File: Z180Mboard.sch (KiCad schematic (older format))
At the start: 66 parts, among them J1 Conn_02x05_Odd_Even, J10 PS2-MINIDIN6-FEMALE-SINGLE, J11 Conn_02x04_Odd_Even, J12 Conn_01x06, J13 Conn_01x06, J14 Conn_02x10_Top_Bottom, J15 Conn_02x05_Odd_Even, J16 DB9_Female, J17 Conn_01x40, J2 Conn_02x05_Odd_Even, J3 Conn_02x05_Odd_Even, J4 Conn_02x05_Odd_Even, J5 Conn_02x05_Odd_Even, J6 Conn_02x05_Odd_Even, J7 Conn_02x05_Odd_Even, J8 Conn_01x08, J9 PS2-MINIDIN6-FEMALE-SINGLE, SW1 SW_SPST, SW2 SW_Push, U1 Z8-L180-S180-180-PLCC-68, U10 74LVC245, U11 DS1307+, U2 SST39SF040, U3 74AHCT138, U4 74AHCT139, U5 AS6C4008-55PCN, U6 AS6C4008-55PCN, U7 82C55A_PLCC, U8 74HCT138, U9 74AHCT151, X1 CXO_DIP8, Y1 Crystal

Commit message: z180mboard: Add the floppy disk interface
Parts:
- added C12, C13, C14: 0.1uF, Capacitor_THT:C_Disc_D3.0mm_W2.0mm_P2.50mm, symbol Device:C
- added J18: Conn_02x17_Odd_Even, Connector_IDC:IDC-Header_2x17_P2.54mm_Vertical, symbol Connector_Generic:Conn_02x17_Odd_Even
- added J19: Conn_01x03, Connector_PinHeader_2.54mm:PinHeader_1x03_P2.54mm_Vertical, symbol Connector_Generic:Conn_01x03
- added JP3: Jumper_3_Open, Connector_PinHeader_2.54mm:PinHeader_1x03_P2.54mm_Vertical, symbol Jumper:Jumper_3_Open
- added R10, R11, R12, R8, R9: 1K, Resistor_THT:R_Axial_DIN0207_L6.3mm_D2.5mm_P7.62mm_Horizontal, symbol Device:R
- added U12: WD37C65C-DIP44, Package_LCC:PLCC-44_THT-Socket, symbol AlanMisc:WD37C65C-DIP44
- added U13: 74HCT138, Package_DIP:DIP-16_W7.62mm_Socket, symbol 74xx:74LS138
- added U14: 74HCT00, Package_DIP:DIP-14_W7.62mm_Socket, symbol 74xx:74HCT00
- added X2: CXO_DIP8, Oscillator:Oscillator_DIP-8, symbol Oscillator:CXO_DIP8
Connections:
- net A0: now also U12.4 (A0), U13.1 (A0)
- net A1: now also U13.2 (A1)
- net A2: now also U13.3 (A2)
- net D0: now also U12.7 (DB0)
- net D1: now also U12.8 (DB1)
- net D2: now also U12.9 (DB2)
- net D3: now also U12.10 (DB3)
- net D4: now also U12.11 (DB4)
- net D5: now also U12.12 (DB5)
- net D6: now also U12.13 (DB6)
- net D7: now also U12.14 (DB7)
- net GND: now also C12.2, C13.2, C14.2, J18.1 (Pin_1), J18.11 (Pin_11), J18.13 (Pin_13), J18.15 (Pin_15), J18.17 (Pin_17), J18.19 (Pin_19), J18.21 (Pin_21), J18.23 (Pin_23), J18.25 (Pin_25), J18.27 (Pin_27), J18.29 (Pin_29), J18.31 (Pin_31), J18.33 (Pin_33), J18.5 (Pin_5), J18.7 (Pin_7), J18.9 (Pin_9), J19.1 (Pin_1), JP3.3 (B), U12.17 (DCHGEN), U12.34 (VSS), U13.4 (E1), U13.8 (GND), U14.12, U14.13, U14.7 (GND), X2.4 (GND)
- net RD: now also U12.1 (RD)
- net RESET: now also U14.9
- net VCC: now also C12.1, C13.1, C14.1, J19.3 (Pin_3), JP3.1 (A), R10.1, R11.1, R12.1, R8.1, R9.1, U12.27 (PCVAL), U12.44 (VCC), U12.6 (TC), U13.16 (VCC), U13.6 (E3), U14.14 (VCC), X2.8 (Vcc)
- net WR: now also U12.2 (WR)
- net FDCEN: now reaches U3.9 (O6)
- net FDCEN: now also U13.5 (E2)
- new net: U12.18 (LDOR), U13.13 (O2)
- new net: U12.19 (LDCR), U13.12 (O3)
- new net: U12.20 (RST), U14.8
- new net: JP3.2 (C), U12.24 (DRV)
- new net: U12.3 (CS), U14.6
- new net: U12.5 (DACK), U13.11 (O4)
- new net: U13.10 (O5), U14.10
- new net: U13.14 (O1), U14.2
- new net: U13.15 (O0), U14.1
- new net: U14.3, U14.4, U14.5
- new net DIR: J18.18 (Pin_18), U12.31 (DIRC)
- new net DRVSA: J18.14 (Pin_14), U12.33 (DS1)
- new net DRVSB: J18.12 (Pin_12), U12.35 (DS2)
- new net DSKCHG: J18.34 (Pin_34), R12.2, U12.40 (DCHG)
- new net FDCLK: U12.26 (XT1), X2.5 (OUT)
- new net FDCLK2: J19.2 (Pin_2), U12.23 (XT2)
- new net INDEX: J18.8 (Pin_8), R8.2, U12.43 (IDX)
- new net MOTEA: J18.10 (Pin_10), U12.36 (MO1/DS3)
- new net MOTEB: J18.16 (Pin_16), U12.37 (MO2/DS4)
- new net RDATA: J18.30 (Pin_30), R11.2, U12.21 (RDD)
- new net REDWC: J18.2 (Pin_2), U12.39 (RWC/RPM)
- new net SIDE1: J18.32 (Pin_32), U12.28 (HS)
- new net STEP: J18.20 (Pin_20), U12.32 (STEP)
- new net TRK00: J18.26 (Pin_26), R9.2, U12.42 (TR00)
- new net WDATA: J18.22 (Pin_22), U12.30 (WD)
- new net WGATE: J18.24 (Pin_24), U12.29 (WE)
- new net WPT: J18.28 (Pin_28), R10.2, U12.41 (WP)
- no-connect marks 58 -> 69
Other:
- note added: "78-7F: PPA\n70-77: FDC\n"
- moved on the sheet: C1, C10, C11, C2, C3, C4, C5, C6, C7, C8, C9, U4C

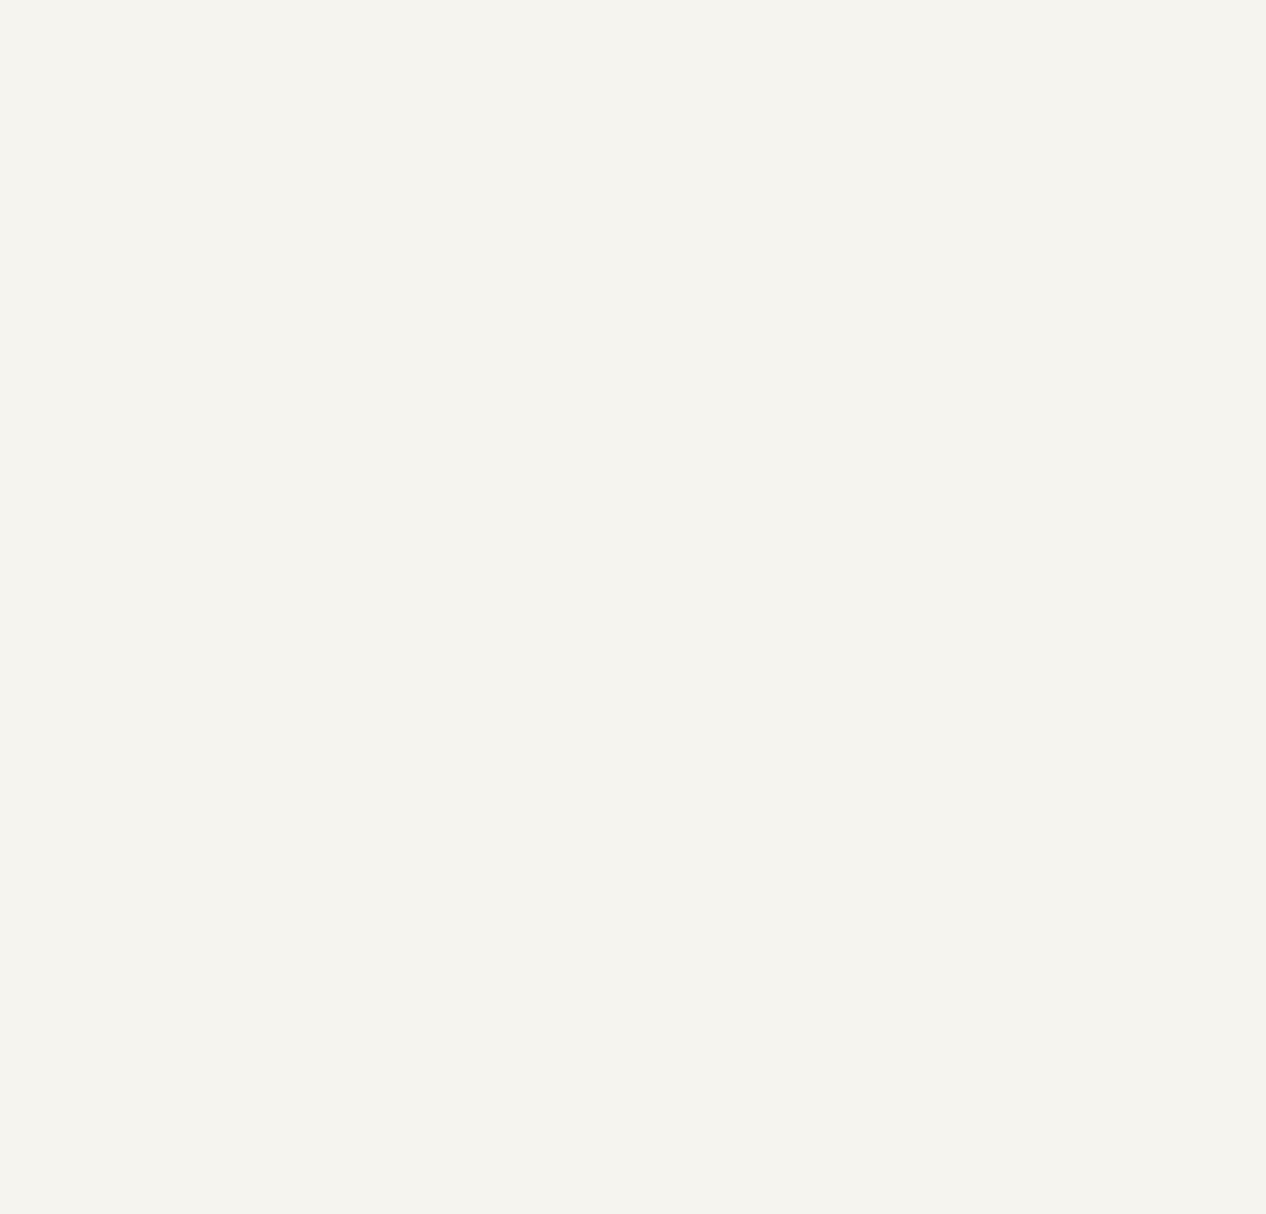
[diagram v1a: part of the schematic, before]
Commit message: z180mboard: pack things in more tightly, turn the battery vertical
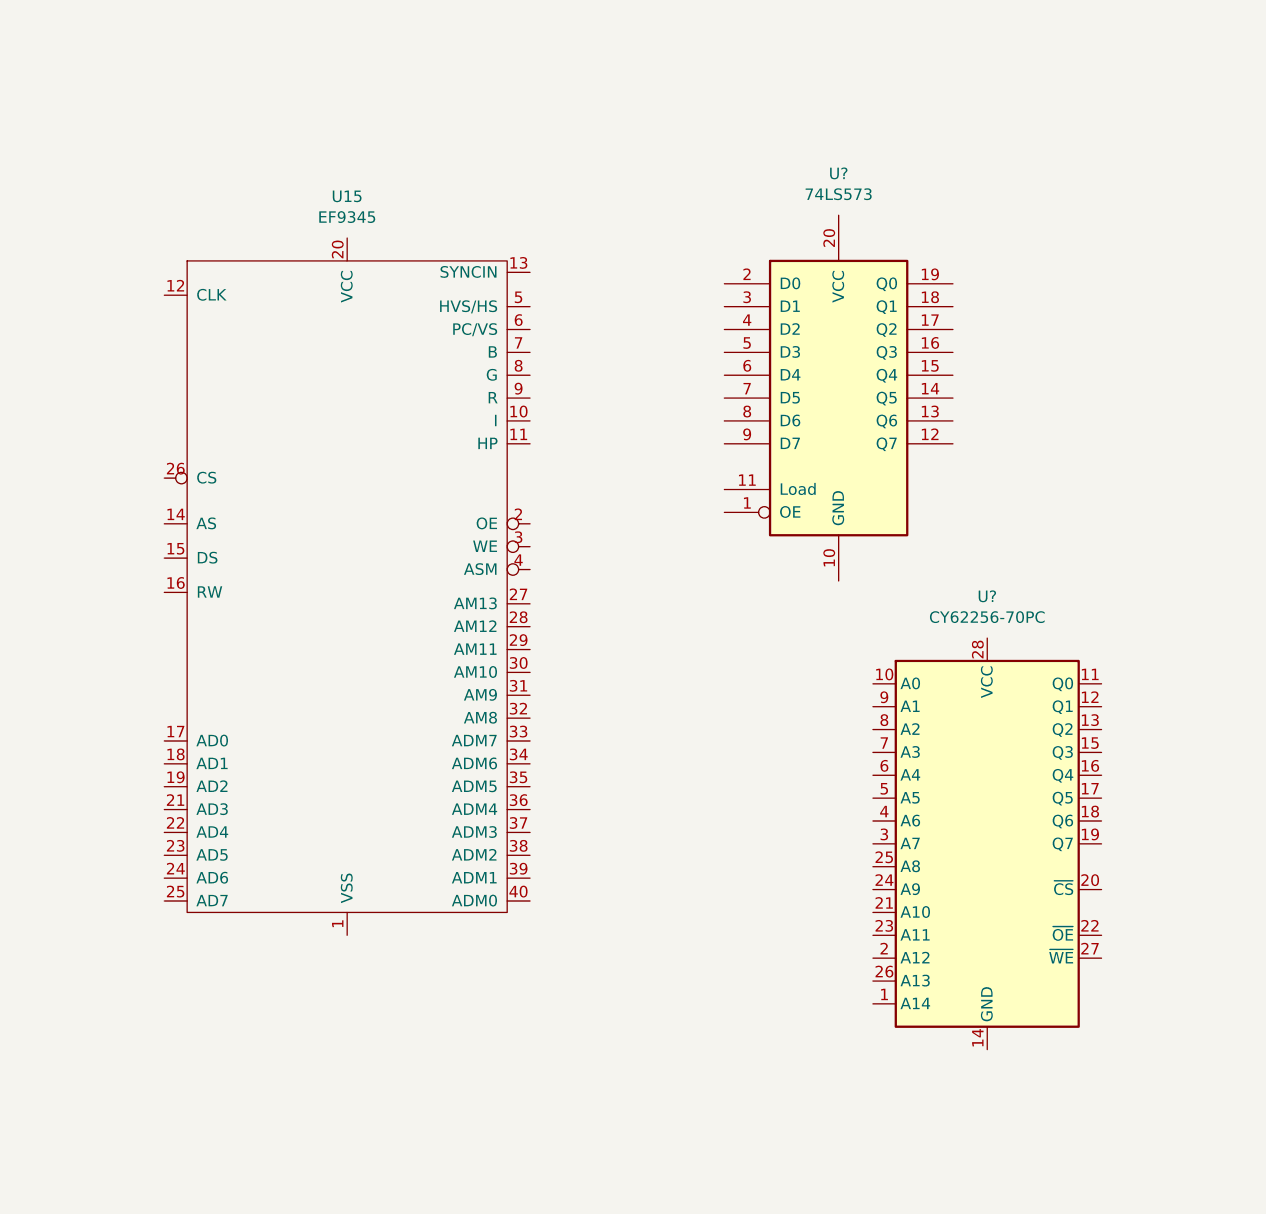
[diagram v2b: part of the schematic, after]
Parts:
- added U15: EF9345, Package_DIP:DIP-40_W15.24mm, symbol AlanMisc:EF9345
- added U?: 74LS573, symbol 74xx:74LS573
- added U?: CY62256-70PC, Package_DIP:DIP-28_W15.24mm, symbol Memory_RAM:CY62256-70PC
- BT1: footprint Battery:BatteryHolder_Keystone_106_1x20mm -> Battery:Battery_Panasonic_CR2032-VS1N_Vertical_CircularHoles
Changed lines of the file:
@@
 F 0 "BT1" H 14418 1596 50  0000 L CNN
 F 1 "Battery_Cell" H 14418 1505 50  0000 L CNN
-F 2 "Battery:BatteryHolder_Keystone_106_1x20mm" V 14300 1560 50  0001 C CNN
+F 2 "Battery:Battery_Panasonic_CR2032-VS1N_Vertical_CircularHoles" V 14300 1560 50  0001 C CNN
 F 3 "~" V 14300 1560 50  0001 C CNN
 	1    14300 1500
@@
 Wire Wire Line
 	7550 22150 8150 22150
+$Comp
+L AlanMisc:EF9345 U15
+U 1 1 6280FCCC
+P 11550 14150
+F 0 "U15" H 11550 15881 50  0000 C CNN
+F 1 "EF9345" H 11550 15790 50  0000 C CNN
+F 2 "Package_DIP:DIP-40_W15.24mm" H 11500 14100 50  0001 C CNN
+F 3 "" H 11500 14100 50  0001 C CNN
+	1    11550 14150
+	1    0    0    -1
+$EndComp
+$Comp
+L 74xx:74LS573 U?
+U 1 1 6284D770
+P 13700 13300
+F 0 "U?" H 13700 14281 50  0000 C CNN
+F 1 "74LS573" H 13700 14190 50  0000 C CNN
+F 2 "" H 13700 13300 50  0001 C CNN
+F 3 "74xx/74hc573.pdf" H 13700 13300 50  0001 C CNN
+	1    13700 13300
+	1    0    0    -1
+$EndComp
+$Comp
+L Memory_RAM:CY62256-70PC U?
+U 1 1 628502E0
+P 14350 15250
+F 0 "U?" H 14350 16331 50  0000 C CNN
+F 1 "CY62256-70PC" H 14350 16240 50  0000 C CNN
+F 2 "Package_DIP:DIP-28_W15.24mm" H 14350 15150 50  0001 C CNN
+F 3 "https://ecee.colorado.edu/~mcclurel/Cypress_SRAM_CY62256.pdf" H 14350 15150 50  0001 C CNN
+	1    14350 15250
+	1    0    0    -1
+$EndComp
 $EndSCHEMATC

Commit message: z180mboard; Add video, holes tidy stuff up
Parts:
- removed U15: EF9345, Package_DIP:DIP-40_W15.24mm, symbol AlanMisc:EF9345
- removed U?: 74LS573, symbol 74xx:74LS573
- removed U?: CY62256-70PC, Package_DIP:DIP-28_W15.24mm, symbol Memory_RAM:CY62256-70PC
- added C15: 0.1uF, Capacitor_THT:C_Disc_D3.0mm_W2.0mm_P2.50mm, symbol Device:C
- added C16: 0.1nF, Capacitor_THT:C_Disc_D3.0mm_W2.0mm_P2.50mm, symbol Device:C
- added C17, C18: C, Capacitor_THT:C_Disc_D3.0mm_W2.0mm_P2.50mm, symbol Device:C
- added J20: Conn_01x06, Connector_PinSocket_2.54mm:PinSocket_1x06_P2.54mm_Vertical, symbol Connector_Generic:Conn_01x06
- added J21: Conn_01x06, Connector_PinHeader_2.54mm:PinHeader_1x06_P2.54mm_Vertical, symbol Connector_Generic:Conn_01x06
- added J22: Conn_Coaxial, Connector_Coaxial:BNC_Amphenol_B6252HB-NPP3G-50_Horizontal, symbol Connector:Conn_Coaxial
- added J23: Conn_01x05, Connector_PinHeader_2.54mm:PinHeader_1x05_P2.54mm_Vertical, symbol Connector_Generic:Conn_01x05
- added JP4: Jumper_3_Open, Connector_PinHeader_2.54mm:PinHeader_1x03_P2.54mm_Vertical, symbol Jumper:Jumper_3_Open
- added R13: 47K, Resistor_THT:R_Axial_DIN0207_L6.3mm_D2.5mm_P7.62mm_Horizontal, symbol Device:R
- added R14: 810, Resistor_THT:R_Axial_DIN0207_L6.3mm_D2.5mm_P7.62mm_Horizontal, symbol Device:R
- added R15, R16, R17: 220, Resistor_THT:R_Axial_DIN0207_L6.3mm_D2.5mm_P7.62mm_Horizontal, symbol Device:R
- added R18: 270, Resistor_THT:R_Axial_DIN0207_L6.3mm_D2.5mm_P7.62mm_Horizontal, symbol Device:R
- added R19: 100, Resistor_THT:R_Axial_DIN0207_L6.3mm_D2.5mm_P7.62mm_Horizontal, symbol Device:R
- added RV1: R_POT, Potentiometer_THT:Potentiometer_Vishay_T7-YA_Single_Vertical, symbol Device:R_POT
- added U15: STV5348, Package_DIP:DIP-28_W15.24mm, symbol Alan:STV5347
- added Y2: 13.875MHz, Crystal:Crystal_C26-LF_D2.1mm_L6.5mm_Vertical, symbol Device:Crystal
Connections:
- net CTS_0: now also J20.2 (Pin_2)
- net GND: now also C15.2, C16.2, C17.1, C18.1, J20.1 (Pin_1), J21.2 (Pin_2), J22.2 (Ext), J23.3 (Pin_3), JP4.1 (A), R13.2, U15.2 (MA/SL), U15.21 (VCR/TV), U15.25 (VSSO), U15.26 (VSSA), U15.27 (TEST), U15.7 (VSS)
- net RESET: now also J20.6 (Pin_6)
- net RX_0: now also J20.4 (Pin_4)
- net SCL_IN: now also U15.16 (SCL)
- net SDA_IN: now also U15.17 (SDA)
- net TX_0: now also J20.5 (Pin_5)
- net VCC: now also C16.1, J20.3 (Pin_3), J21.1 (Pin_1), JP4.3 (B), U15.11 (RGBREF), U15.22 (VDD), U15.3 (VDDA)
- new net: R13.1, U15.20 (TEST)
- new net: C17.2, U15.23 (XTO), Y2.1
- new net: C18.2, U15.24 (XTI), Y2.2
- new net: C15.1, U15.28 (CBLK)
- new net: JP4.2 (C), U15.4 (POL)
- new net: J22.1 (In), R14.1, R19.2
- new net: J21.6 (Pin_6), R15.1
- new net: J21.5 (Pin_5), R16.1
- new net: J21.4 (Pin_4), R17.1
- new net: J21.3 (Pin_3), R18.2
- new net: R19.1, RV1.3
- new net B: J23.4 (Pin_4), R17.2, U15.10 (B)
- new net CSYNC: J23.1 (Pin_1), R18.1, RV1.2, U15.5 (STTV/LFB)
- new net G: J23.2 (Pin_2), R14.2, R16.2, U15.9 (G)
- new net R: J23.5 (Pin_5), R15.2, U15.8 (R)
- no-connect marks 69 -> 78
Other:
- note added: "78-7F: PPA\n70-77: FDC\n68-6F: VID\n"
- note removed: "78-7F: PPA\n70-77: FDC\n"
- moved on the sheet: C1, C10, C11, C12, C13, C14, C2, C3, C4, C5, C6, C7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

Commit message: Z180Mboard: more cleaning up and connector add
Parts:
- added J24: Conn_01x15, Connector_PinSocket_2.54mm:PinSocket_1x15_P2.54mm_Vertical, symbol Connector_Generic:Conn_01x15
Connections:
- net +3V3: now also J24.5 (Pin_5)
- net EXTMEM: now also J24.1 (Pin_1)
- net GND: now also J24.11 (Pin_11), J24.13 (Pin_13), J24.15 (Pin_15), J24.7 (Pin_7), J24.9 (Pin_9)
- net SCL_IN: now also J24.4 (Pin_4)
- net SDA_IN: now also J24.3 (Pin_3)
- net VCC: now also J24.2 (Pin_2)
- no-connect marks 78 -> 83
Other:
- note added: "78-7F: PPA\n70-77: FDC\n\n"
- note removed: "78-7F: PPA\n70-77: FDC\n68-6F: VID\n"
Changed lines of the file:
@@
 	6200 22600 6800 22600
 Text Notes 12500 4700 0    50   ~ 0
-78-7F: PPA\n70-77: FDC\n68-6F: VID\n
+78-7F: PPA\n70-77: FDC\n\n
 Wire Wire Line
 	9100 20700 9100 20900
@@
 Wire Wire Line
 	11050 14650 11050 15500
+Text GLabel 13500 2450 0    50   Input ~ 0
+EXTMEM
+$Comp
+L power:GND #PWR0164
+U 1 1 6383E07D
+P 13500 4250
+F 0 "#PWR0164" H 13500 4000 50  0001 C CNN
+F 1 "GND" H 13505 4077 50  0000 C CNN
+F 2 "" H 13500 4250 50  0001 C CNN
+F 3 "" H 13500 4250 50  0001 C CNN
+	1    13500 4250
+	1    0    0    -1
+$EndComp
+Wire Wire Line
+	13500 3850 13500 4250
+$Comp
+L Connector_Generic:Conn_01x15 J24
+U 1 1 6380471E
+P 13700 3150
+F 0 "J24" H 13780 3192 50  0000 L CNN
+F 1 "Conn_01x15" H 13780 3101 50  0000 L CNN
+F 2 "Connector_PinSocket_2.54mm:PinSocket_1x15_P2.54mm_Vertical" H 13700 3150 50  0001 C CNN
+F 3 "~" H 13700 3150 50  0001 C CNN
+	1    13700 3150
+	1    0    0    -1
+$EndComp
+Wire Wire Line
+	13500 3650 13300 3650
+Wire Wire Line
+	13300 3650 13300 3850
+Wire Wire Line
+	13300 3850 13500 3850
+Connection ~ 13500 3850
+Wire Wire Line
+	13300 3650 13300 3450
+Wire Wire Line
+	13300 3450 13500 3450
+Connection ~ 13300 3650
+Wire Wire Line
+	13300 3450 13300 3250
+Wire Wire Line
+	13300 3250 13500 3250
+Connection ~ 13300 3450
+Wire Wire Line
+	13300 3250 13300 3050
+Wire Wire Line
+	13300 3050 13500 3050
+Connection ~ 13300 3250
+Text GLabel 13500 2550 0    50   Input ~ 0
+VCC
+Text GLabel 13500 2650 0    50   3State ~ 0
+SDA_LINE
+Text GLabel 13500 2750 0    50   3State ~ 0
+SCL_LINE
+Text GLabel 13500 2850 0    50   3State ~ 0
+3V3
+NoConn ~ 13500 3750
+NoConn ~ 13500 3550
+NoConn ~ 13500 3350
+NoConn ~ 13500 3150
+NoConn ~ 13500 2950
 $EndSCHEMATC

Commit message: Notes for bugs/mods for v2/v3
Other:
- note added: "FIXME: Add surface mount footprint as well"
- note added: "FIXME: DC is a 5v signal this is a 3v3 slot!\n"
- note added: "FIXME: Move to 40-4F to match EDFDC\nand clear space for extmem to be useful"
- note added: "FIXME: Swap DC and EXTMEM over"
- note added: "FIXME: change EXTMEM to instead control external MREQ on high address range."
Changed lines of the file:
@@
 NoConn ~ 13500 3150
 NoConn ~ 13500 2950
+Text Notes 950  5000 0    50   ~ 10
+FIXME: DC is a 5v signal this is a 3v3 slot!\n
+Text Notes 14200 8650 0    50   ~ 0
+FIXME: Swap DC and EXTMEM over
+Text Notes 9950 11100 0    50   ~ 0
+FIXME: Add surface mount footprint as well
+Text Notes 12400 4850 0    50   ~ 0
+FIXME: Move to 40-4F to match EDFDC\nand clear space for extmem to be useful
+Text Notes 9450 3850 0    50   ~ 0
+FIXME: change EXTMEM to instead control external MREQ on high address range.
 $EndSCHEMATC
